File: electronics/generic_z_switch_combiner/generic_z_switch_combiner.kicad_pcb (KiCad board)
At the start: 2 copper layers, 18 x 14.5 mm, 7 parts, among them J1 Conn_01x02, J2 Conn_01x02, J3 Conn_01x02

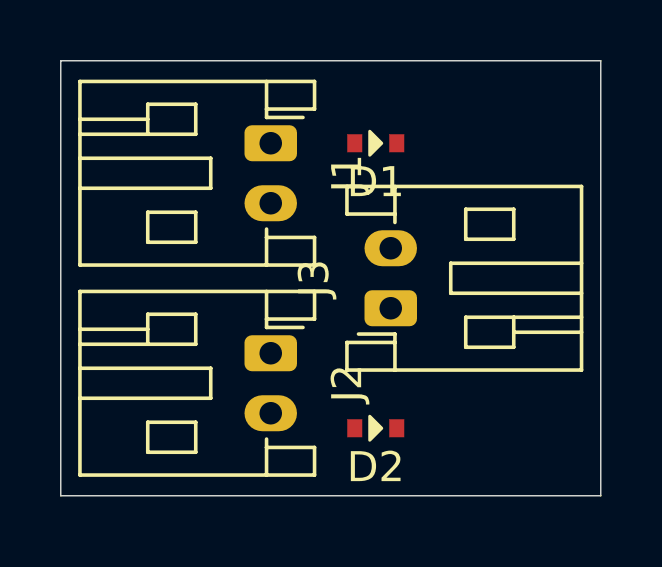
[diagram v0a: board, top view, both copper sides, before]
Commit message: updated versionnumber and routed traces
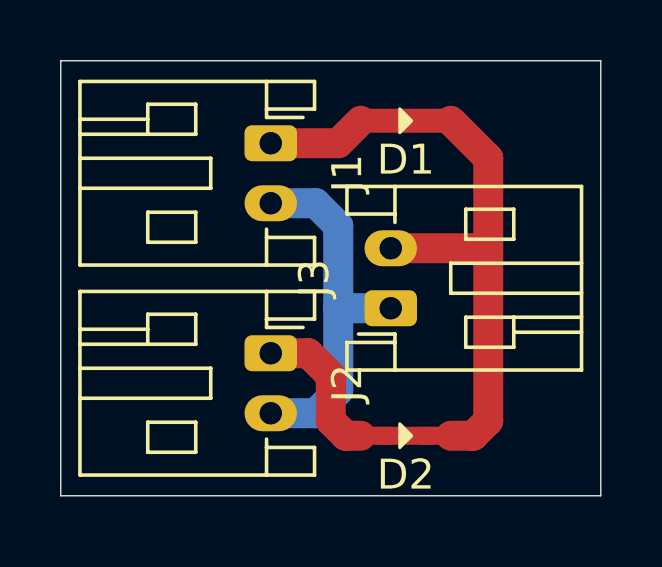
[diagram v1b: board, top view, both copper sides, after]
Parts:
- N1: value 20200611 -> 20200615
- moved D1 1.25 mm to (139.5, 65.2)
- moved D2 1.03 mm to (139.5, 75.8)
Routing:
- net Net-(D1-Pad1): track 0.00 -> 29.6 mm
- net Net-(J1-Pad2): track 0.00 -> 12.4 mm
